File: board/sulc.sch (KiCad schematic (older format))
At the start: 51 parts, among them J1 LED_PWR, J2 HWB, P1 USB, P14 CONN_1, P2 LED+, P20 CONN_1, P3 RED, P4 GREEN, P5 BLUE, P7 ISP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

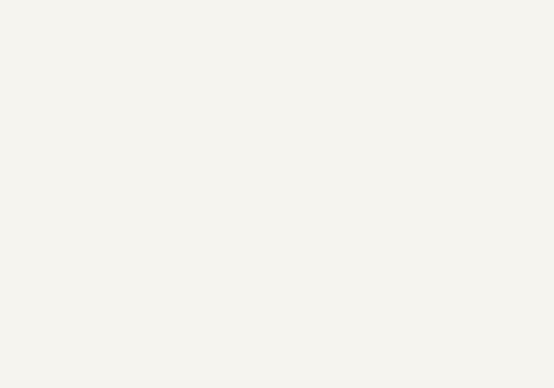
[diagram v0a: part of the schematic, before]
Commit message: Added mounting holes. Bigger footprint for C1.
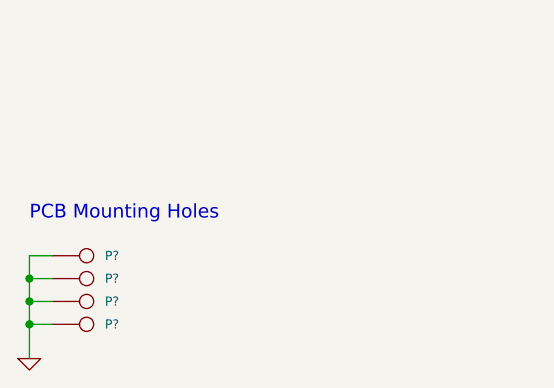
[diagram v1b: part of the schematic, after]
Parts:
- added P? (x4): CONN_1, symbol CONN_1
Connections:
- wire segments 244 -> 249
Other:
- note added: "PCB Mounting Holes"
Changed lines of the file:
@@
-EESchema Schematic File Version 2  date Monday, March 26, 2012 03:55:15 PM
+EESchema Schematic File Version 2  date Wednesday, March 28, 2012 02:14:53 PM
 LIBS:power
 LIBS:device
@@
 Sheet 1 1
 Title "SULC - Simple USB LED Controller"
-Date "26 mar 2012"
+Date "28 mar 2012"
 Rev ""
 Comp "Scott Bezek (scottbezek.com)"
@@
 Comment4 ""
 $EndDescr
+Connection ~ 1350 6650
+Wire Wire Line
+	1350 6650 1450 6650
+Connection ~ 1350 6450
+Wire Wire Line
+	1350 6450 1450 6450
 Wire Wire Line
 	6800 700  6800 650
@@
 	6800 5300 6800 1200
 Connection ~ 6800 1750
+Wire Wire Line
+	1350 6800 1350 6350
+Wire Wire Line
+	1350 6350 1450 6350
+Wire Wire Line
+	1350 6550 1450 6550
+Connection ~ 1350 6550
+$Comp
+L CONN_1 P?
+U 1 1 4F73550B
+P 1600 6650
+F 0 "P?" H 1680 6650 40  0000 L CNN
+F 1 "CONN_1" H 1600 6705 30  0001 C CNN
+	1    1600 6650
+	1    0    0    -1
+$EndComp
+$Comp
+L CONN_1 P?
+U 1 1 4F735505
+P 1600 6550
+F 0 "P?" H 1680 6550 40  0000 L CNN
+F 1 "CONN_1" H 1600 6605 30  0001 C CNN
+	1    1600 6550
+	1    0    0    -1
+$EndComp
+$Comp
+L CONN_1 P?
+U 1 1 4F735502
+P 1600 6450
+F 0 "P?" H 1680 6450 40  0000 L CNN
+F 1 "CONN_1" H 1600 6505 30  0001 C CNN
+	1    1600 6450
+	1    0    0    -1
+$EndComp
+$Comp
+L CONN_1 P?
+U 1 1 4F7354F5
+P 1600 6350
+F 0 "P?" H 1680 6350 40  0000 L CNN
+F 1 "CONN_1" H 1600 6405 30  0001 C CNN
+	1    1600 6350
+	1    0    0    -1
+$EndComp
+$Comp
+L GND #PWR?
+U 1 1 4F7354EA
+P 1350 6800
+F 0 "#PWR?" H 1350 6800 30  0001 C CNN
+F 1 "GND" H 1350 6730 30  0001 C CNN
+	1    1350 6800
+	1    0    0    -1
+$EndComp
+Text Notes 1350 6200 0    60   ~ 0
+PCB Mounting Holes
 $Comp
 L +5V #PWR?
